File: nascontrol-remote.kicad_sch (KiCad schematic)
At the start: 22 parts, among them J101 Serial, J102 System IN, J103 Control, J104 System OUT, U101 EL817, U102 EL817, U103 EL817, U104 EL817

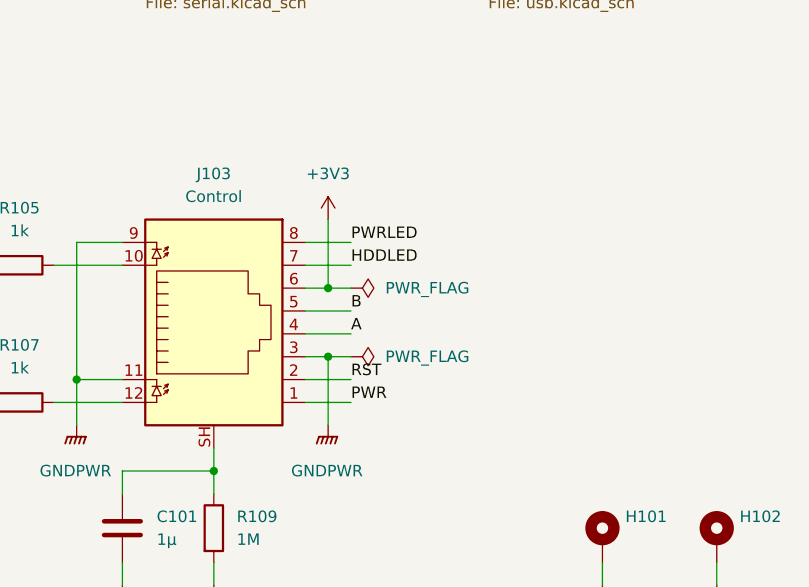
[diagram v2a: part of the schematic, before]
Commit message: Inverse RJ45 connections
Signed-off-by: Benedikt Spranger <b.spranger@linutronix.de>
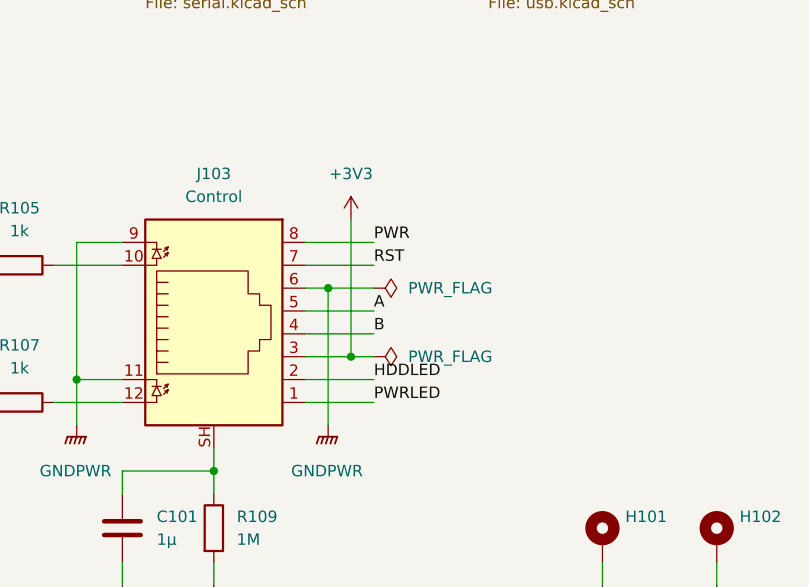
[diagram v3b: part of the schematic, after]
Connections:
- net +3V3: now also J103.3; no longer J103.6
- net A: now also J103.5; no longer J103.4
- net B: now also J103.4; no longer J103.5
- net GNDPWR: now also J103.6; no longer J103.3
- net HDDLED: now also J103.2; no longer J103.7
- net PWR: now also J103.8; no longer J103.1
- net PWRLED: now also J103.1; no longer J103.8
- net RST: now also J103.7; no longer J103.2
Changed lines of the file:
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@@
   (junction (at 118.11 134.62) (diameter 0) (color 0 0 0 0)
   )
-  (junction (at 210.82 116.84) (diameter 0) (color 0 0 0 0)
-  )
   (junction (at 182.88 119.38) (diameter 0) (color 0 0 0 0)
   )
   (junction (at 135.89 96.52) (diameter 0) (color 0 0 0 0)
   )
+  (junction (at 213.36 116.84) (diameter 0) (color 0 0 0 0)
+  )
   (junction (at 68.58 165.1) (diameter 0) (color 0 0 0 0)
   )
+  (junction (at 210.82 109.22) (diameter 0) (color 0 0 0 0)
+  )
   (junction (at 118.11 96.52) (diameter 0) (color 0 0 0 0)
   )
@@
   )
   (junction (at 135.89 134.62) (diameter 0) (color 0 0 0 0)
-  )
-  (junction (at 210.82 109.22) (diameter 0) (color 0 0 0 0)
   )
   (no_connect (at 120.65 60.96))
@@
     (stroke (width 0) (type default))
   )
-  (wire (pts (xy 210.82 116.84) (xy 213.36 116.84))
-    (stroke (width 0) (type default))
-  )
   (wire (pts (xy 180.34 106.68) (xy 187.96 106.68))
     (stroke (width 0) (type default))
@@
     (stroke (width 0) (type default))
   )
-  (wire (pts (xy 208.28 111.76) (xy 213.36 111.76))
+  (wire (pts (xy 208.28 111.76) (xy 215.9 111.76))
     (stroke (width 0) (type default))
   )
@@
     (stroke (width 0) (type default))
   )
+  (wire (pts (xy 208.28 109.22) (xy 210.82 109.22))
+    (stroke (width 0) (type default))
+  )
   (wire (pts (xy 187.96 53.34) (xy 190.5 53.34))
     (stroke (width 0) (type default))
   )
-  (wire (pts (xy 208.28 121.92) (xy 213.36 121.92))
+  (wire (pts (xy 208.28 121.92) (xy 215.9 121.92))
     (stroke (width 0) (type default))
   )
@@
     (stroke (width 0) (type default))
   )
+  (wire (pts (xy 213.36 101.6) (xy 213.36 116.84))
+    (stroke (width 0) (type default))
+  )
   (wire (pts (xy 187.96 139.7) (xy 187.96 142.24))
     (stroke (width 0) (type default))
@@
     (stroke (width 0) (type default))
   )
-  (wire (pts (xy 210.82 109.22) (xy 210.82 101.6))
-    (stroke (width 0) (type default))
-  )
   (wire (pts (xy 180.34 121.92) (xy 187.96 121.92))
     (stroke (width 0) (type default))
@@
     (stroke (width 0) (type default))
   )
-  (wire (pts (xy 208.28 104.14) (xy 213.36 104.14))
+  (wire (pts (xy 208.28 104.14) (xy 215.9 104.14))
     (stroke (width 0) (type default))
   )
@@
     (stroke (width 0) (type default))
   )
-  (wire (pts (xy 210.82 109.22) (xy 213.36 109.22))
-    (stroke (width 0) (type default))
-  )
   (wire (pts (xy 118.11 55.88) (xy 118.11 63.5))
     (stroke (width 0) (type default))
@@
     (stroke (width 0) (type default))
   )
-  (wire (pts (xy 208.28 119.38) (xy 213.36 119.38))
+  (wire (pts (xy 208.28 119.38) (xy 215.9 119.38))
     (stroke (width 0) (type default))
   )
@@
     (stroke (width 0) (type default))
   )
-  (wire (pts (xy 210.82 116.84) (xy 210.82 124.46))
-    (stroke (width 0) (type default))
-  )
   (wire (pts (xy 187.96 63.5) (xy 190.5 63.5))
     (stroke (width 0) (type default))
@@
     (stroke (width 0) (type default))
   )
+  (wire (pts (xy 210.82 109.22) (xy 215.9 109.22))
+    (stroke (width 0) (type default))
+  )
   (wire (pts (xy 118.11 96.52) (xy 118.11 99.06))
     (stroke (width 0) (type default))
@@
     (stroke (width 0) (type default))
   )
-  (wire (pts (xy 208.28 114.3) (xy 213.36 114.3))
+  (wire (pts (xy 208.28 114.3) (xy 215.9 114.3))
     (stroke (width 0) (type default))
   )
@@
     (stroke (width 0) (type default))
   )
-  (wire (pts (xy 208.28 106.68) (xy 213.36 106.68))
+  (wire (pts (xy 208.28 106.68) (xy 215.9 106.68))
     (stroke (width 0) (type default))
   )
@@
     (stroke (width 0) (type default))
   )
-  (wire (pts (xy 208.28 116.84) (xy 210.82 116.84))
+  (wire (pts (xy 208.28 116.84) (xy 213.36 116.84))
     (stroke (width 0) (type default))
   )
@@
     (stroke (width 0) (type default))
   )
-  (wire (pts (xy 208.28 109.22) (xy 210.82 109.22))
-    (stroke (width 0) (type default))
-  )
   (wire (pts (xy 48.26 88.9) (xy 50.8 88.9))
     (stroke (width 0) (type default))
@@
     (stroke (width 0) (type default))
   )
+  (wire (pts (xy 210.82 109.22) (xy 210.82 124.46))
+    (stroke (width 0) (type default))
+  )
   (wire (pts (xy 66.04 132.08) (xy 68.58 132.08))
     (stroke (width 0) (type default))
@@
     (stroke (width 0) (type default))
   )
+  (wire (pts (xy 213.36 116.84) (xy 215.9 116.84))
+    (stroke (width 0) (type default))
+  )
   (wire (pts (xy 115.57 58.42) (xy 120.65 58.42))
     (stroke (width 0) (type default))
@@
     (effects (font (size 1.27 1.27)) (justify right bottom))
   )
-  (label "A" (at 213.36 114.3 0) (fields_autoplaced)
+  (label "A" (at 215.9 111.76 0) (fields_autoplaced)
     (effects (font (size 1.27 1.27)) (justify left bottom))
   )
@@
     (effects (font (size 1.27 1.27)) (justify right bottom))
   )
-  (label "PWRLED" (at 213.36 104.14 0) (fields_autoplaced)
+  (label "PWRLED" (at 215.9 121.92 0) (fields_autoplaced)
     (effects (font (size 1.27 1.27)) (justify left bottom))
   )
@@
     (effects (font (size 1.27 1.27)) (justify right bottom))
   )
-  (label "HDDLED" (at 213.36 106.68 0) (fields_autoplaced)
+  (label "HDDLED" (at 215.9 119.38 0) (fields_autoplaced)
     (effects (font (size 1.27 1.27)) (justify left bottom))
   )
@@
     (effects (font (size 1.27 1.27)) (justify left bottom))
   )
-  (label "B" (at 213.36 111.76 0) (fields_autoplaced)
+  (label "B" (at 215.9 114.3 0) (fields_autoplaced)
     (effects (font (size 1.27 1.27)) (justify left bottom))
   )
@@
     (effects (font (size 1.27 1.27)) (justify left bottom))
   )
-  (label "RST" (at 213.36 119.38 0) (fields_autoplaced)
+  (label "RST" (at 215.9 106.68 0) (fields_autoplaced)
     (effects (font (size 1.27 1.27)) (justify left bottom))
   )
@@
     (effects (font (size 1.27 1.27)) (justify right bottom))
   )
-  (label "PWR" (at 213.36 121.92 0) (fields_autoplaced)
+  (label "PWR" (at 215.9 104.14 0) (fields_autoplaced)
     (effects (font (size 1.27 1.27)) (justify left bottom))
   )
@@
     )
   )
-  (symbol (lib_id "power:+3V3") (at 210.82 101.6 0) (unit 1)
-    (in_bom yes) (on_board yes) (dnp no) (fields_autoplaced)
-    (property "Reference" "#PWR0110" (at 210.82 105.41 0)
-      (effects (font (size 1.27 1.27)) hide)
-    )
-    (property "Value" "+3V3" (at 210.82 96.52 0)
-      (effects (font (size 1.27 1.27)))
-    )
-    (property "Footprint" "" (at 210.82 101.6 0)
-      (effects (font (size 1.27 1.27)) hide)
-    )
-    (property "Datasheet" "" (at 210.82 101.6 0)
+  (symbol (lib_id "power:+3V3") (at 213.36 101.6 0) (unit 1)
+    (in_bom yes) (on_board yes) (dnp no) (fields_autoplaced)
+    (property "Reference" "#PWR0110" (at 213.36 105.41 0)
+      (effects (font (size 1.27 1.27)) hide)
+    )
+    (property "Value" "+3V3" (at 213.36 96.52 0)
+      (effects (font (size 1.27 1.27)))
+    )
+    (property "Footprint" "" (at 213.36 101.6 0)
+      (effects (font (size 1.27 1.27)) hide)
+    )
+    (property "Datasheet" "" (at 213.36 101.6 0)
       (effects (font (size 1.27 1.27)) hide)
     )
@@
     )
   )
-  (symbol (lib_id "power:PWR_FLAG") (at 213.36 116.84 270) (unit 1)
-    (in_bom yes) (on_board yes) (dnp no) (fields_autoplaced)
-    (property "Reference" "#FLG0102" (at 215.265 116.84 0)
-      (effects (font (size 1.27 1.27)) hide)
-    )
-    (property "Value" "PWR_FLAG" (at 217.17 116.8399 90)
+  (symbol (lib_id "power:PWR_FLAG") (at 215.9 116.84 270) (unit 1)
+    (in_bom yes) (on_board yes) (dnp no) (fields_autoplaced)
+    (property "Reference" "#FLG0102" (at 217.805 116.84 0)
+      (effects (font (size 1.27 1.27)) hide)
+    )
+    (property "Value" "PWR_FLAG" (at 219.71 116.8399 90)
       (effects (font (size 1.27 1.27)) (justify left))
     )
-    (property "Footprint" "" (at 213.36 116.84 0)
-      (effects (font (size 1.27 1.27)) hide)
-    )
-    (property "Datasheet" "~" (at 213.36 116.84 0)
+    (property "Footprint" "" (at 215.9 116.84 0)
+      (effects (font (size 1.27 1.27)) hide)
+    )
+    (property "Datasheet" "~" (at 215.9 116.84 0)
       (effects (font (size 1.27 1.27)) hide)
     )
@@
     )
   )
-  (symbol (lib_id "power:PWR_FLAG") (at 213.36 109.22 270) (unit 1)
-    (in_bom yes) (on_board yes) (dnp no) (fields_autoplaced)
-    (property "Reference" "#FLG0101" (at 215.265 109.22 0)
-      (effects (font (size 1.27 1.27)) hide)
-    )
-    (property "Value" "PWR_FLAG" (at 217.17 109.2199 90)
+  (symbol (lib_id "power:PWR_FLAG") (at 215.9 109.22 270) (unit 1)
+    (in_bom yes) (on_board yes) (dnp no) (fields_autoplaced)
+    (property "Reference" "#FLG0101" (at 217.805 109.22 0)
+      (effects (font (size 1.27 1.27)) hide)
+    )
+    (property "Value" "PWR_FLAG" (at 219.71 109.2199 90)
       (effects (font (size 1.27 1.27)) (justify left))
     )
-    (property "Footprint" "" (at 213.36 109.22 0)
-      (effects (font (size 1.27 1.27)) hide)
-    )
-    (property "Datasheet" "~" (at 213.36 109.22 0)
-      (effects (font (size 1.27 1.27)) hide)
-    )
+    (property "Footprint" "" (at 215.9 109.22 0)
+      (effects (font (size 1.27 1.27)) hide)
+    )
+    (property "Datasheet" "~" (at 215.9 109.22 0)
+      (effects (font (size 1.27 1.27)) hide)
+    )
